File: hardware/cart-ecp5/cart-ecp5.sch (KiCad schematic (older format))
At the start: 1 part, among them U1 LFE5U-25F-xBG256x

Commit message: Create a basic N64 cartridge PCB layout
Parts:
- added C1: 10u, Capacitor_SMD:C_0603_1608Metric, symbol Device:C
- added C2: 10n, Capacitor_SMD:C_0402_1005Metric, symbol Device:C
- added C3, C4: 10u, Capacitor_SMD:C_0402_1005Metric, symbol Device:C
- added J1: N64_Cartridge_Bus, ng_n64:N64_Cartridge_Edge, symbol ng_n64:N64_Cartridge_Bus
- added L1: 470n, Inductor_SMD:L_0805_2012Metric, symbol Device:L
- added R1: 240R, Resistor_SMD:R_0603_1608Metric, symbol Device:R
- added R2, R3, R4: 100k, Resistor_SMD:R_0402_1005Metric, symbol Device:R
- added R5: 267k, Resistor_SMD:R_0402_1005Metric, symbol Device:R
- added U2: MT41K64M16TW-xxx, Package_BGA:BGA-96_9.0x13.0mm_Layout2x3x16_P0.8mm, symbol ng_memory:MT41K64M16TW-xxx
- added U3: FAN53541, Package_CSP:WLCSP-20_1.934x2.434mm_Layout4x5_P0.4mm, symbol ng_pmic:FAN53541
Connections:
- net labels added: DRAM_A0, DRAM_A1, DRAM_A10, DRAM_A11, DRAM_A12, DRAM_A13, DRAM_A14, DRAM_A15, DRAM_A2, DRAM_A3, DRAM_A4, DRAM_A5, DRAM_A6, DRAM_A7, DRAM_A8, DRAM_A9, DRAM_BA0, DRAM_BA1, DRAM_BA2, DRAM_CAS#, DRAM_CK+, DRAM_CK-, DRAM_CKE, DRAM_CS#, DRAM_DQ0, DRAM_DQ1, DRAM_DQ10, DRAM_DQ11, DRAM_DQ12, DRAM_DQ13, DRAM_DQ14, DRAM_DQ15, DRAM_DQ2, DRAM_DQ3, DRAM_DQ4, DRAM_DQ5, DRAM_DQ6, DRAM_DQ7, DRAM_DQ8, DRAM_DQ9, DRAM_LDM, DRAM_LDQS+, DRAM_LDQS-, DRAM_ODT, DRAM_RAS#, DRAM_RESET#, DRAM_UDM, DRAM_UDQS+, DRAM_UDQS-, DRAM_VDD, DRAM_VDDQ, DRAM_VREF, DRAM_WE#, DRAM_ZQ, FB1V1, N64_12V, N64_3V3, N64_AD0, N64_AD1, N64_AD10, N64_AD11, N64_AD12, N64_AD13, N64_AD14, N64_AD15, N64_AD2, N64_AD3, N64_AD4, N64_AD5, N64_AD6, N64_AD7, N64_AD8, N64_AD9, N64_ALE_H, N64_ALE_L, N64_AUDIO_L, N64_AUDIO_R, N64_COLD_RESET#, N64_OS_EVENT#, N64_READ#, N64_S_CLK, N64_S_DAT, N64_WRITE#, P3V3, PGOOD_1V1, SW1V1
- wire segments 235 -> 380
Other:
- moved on the sheet: U1A, U1B, U1C, U1D, U1E, U1F, U1G, U1H, U1I

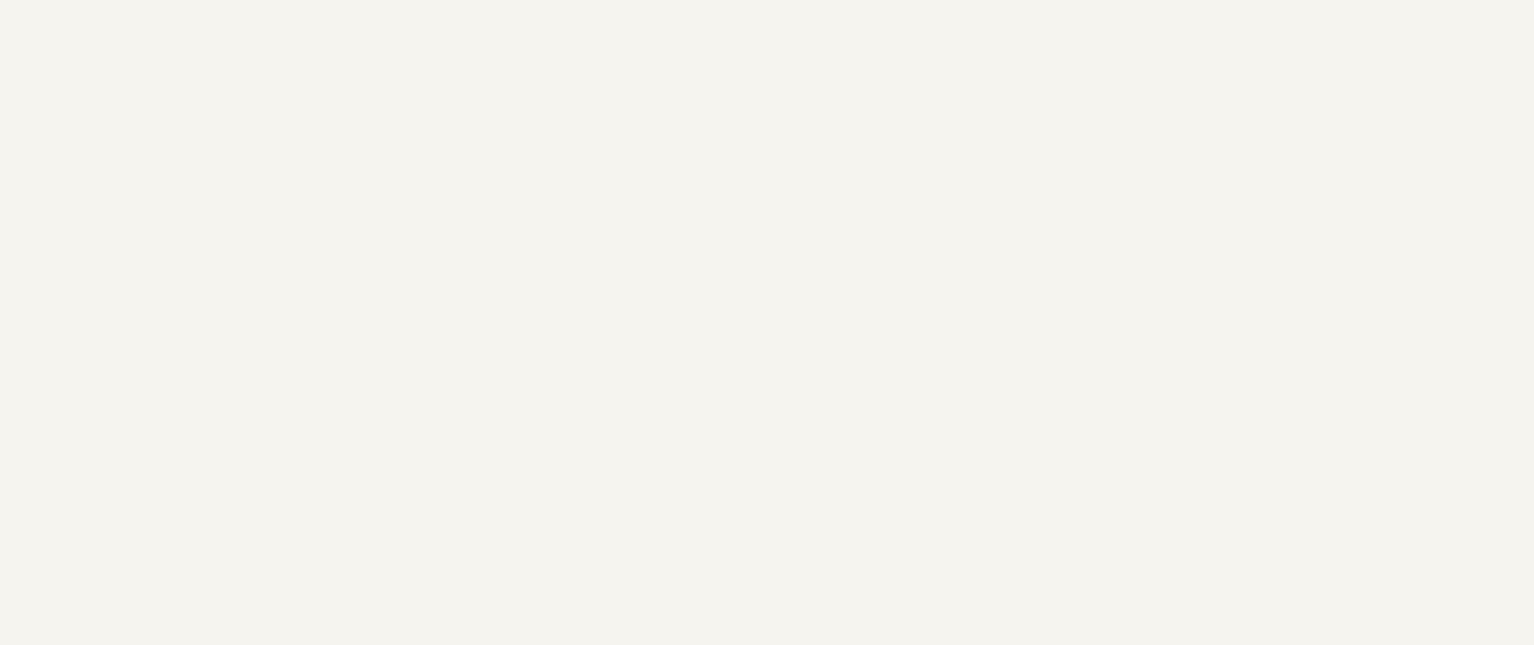
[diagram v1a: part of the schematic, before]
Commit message: Check new HyperRAM symbols on the board
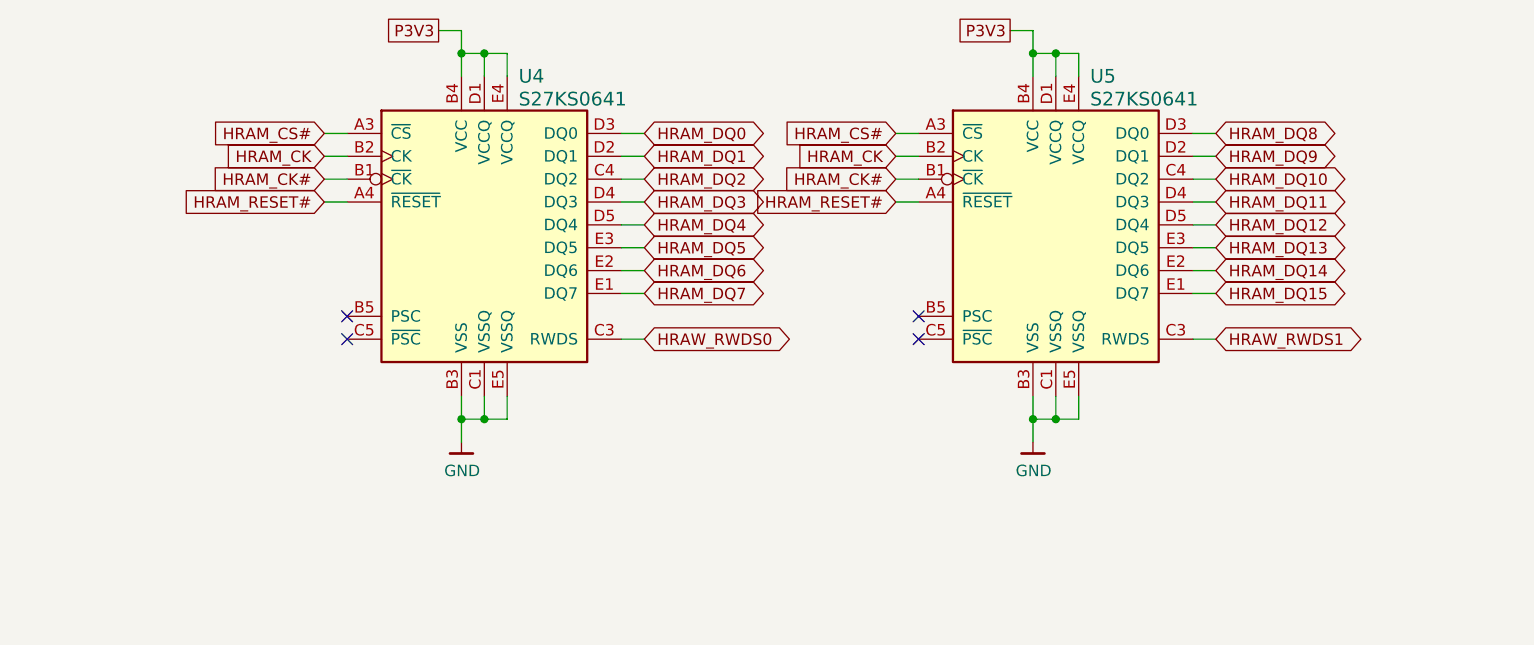
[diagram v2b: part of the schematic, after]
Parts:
- added U4, U5: S27KS0641, ng_package_bga:BGA-24_6.0x8.0mm_Layout5x5_P1.0mm_Pad0.4mm, symbol ng_memory:S27KS0641
- U1: footprint ng_package_bga:BGA-256_16x16_14.0x14.0mm_P0.8mm_Pad0.35mm -> ng_package_bga:BGA-256_14.0x14.0mm_Layout16x16_P0.8mm_Pad0.35mm
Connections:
- net labels added: HRAM_CK, HRAM_CK#, HRAM_CS#, HRAM_DQ0, HRAM_DQ1, HRAM_DQ10, HRAM_DQ11, HRAM_DQ12, HRAM_DQ13, HRAM_DQ14, HRAM_DQ15, HRAM_DQ2, HRAM_DQ3, HRAM_DQ4, HRAM_DQ5, HRAM_DQ6, HRAM_DQ7, HRAM_DQ8, HRAM_DQ9, HRAM_RESET#, HRAW_RWDS0, HRAW_RWDS1
- wire segments 380 -> 432
- no-connect marks 0 -> 4
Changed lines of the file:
@@
 F 0 "U1" H 3681 3553 60  0000 L CNN
 F 1 "LFE5U-25F-xBG256x" H 3681 3447 60  0000 L CNN
-F 2 "ng_package_bga:BGA-256_16x16_14.0x14.0mm_P0.8mm_Pad0.35mm" H 3300 3400 60  0001 R CNN
+F 2 "ng_package_bga:BGA-256_14.0x14.0mm_Layout16x16_P0.8mm_Pad0.35mm" H 3300 3400 60  0001 R CNN
 F 3 "" H 3300 3200 60  0001 R CNN
 F 4 "LFE5U-25F-xBG256x" H 3300 3300 60  0001 R CNN "MPN"
@@
 F 0 "U1" H 4031 5360 60  0000 L CNN
 F 1 "LFE5U-25F-xBG256x" H 4031 5254 60  0000 L CNN
-F 2 "ng_package_bga:BGA-256_16x16_14.0x14.0mm_P0.8mm_Pad0.35mm" H 2750 6100 60  0001 R CNN
+F 2 "ng_package_bga:BGA-256_14.0x14.0mm_Layout16x16_P0.8mm_Pad0.35mm" H 2750 6100 60  0001 R CNN
 F 3 "" H 2750 5900 60  0001 R CNN
 F 4 "LFE5U-25F-xBG256x" H 2750 6000 60  0001 R CNN "MPN"
@@
 F 0 "U1" H 7781 4860 60  0000 L CNN
 F 1 "LFE5U-25F-xBG256x" H 7781 4754 60  0000 L CNN
-F 2 "ng_package_bga:BGA-256_16x16_14.0x14.0mm_P0.8mm_Pad0.35mm" H 6500 6000 60  0001 R CNN
+F 2 "ng_package_bga:BGA-256_14.0x14.0mm_Layout16x16_P0.8mm_Pad0.35mm" H 6500 6000 60  0001 R CNN
 F 3 "" H 6500 5800 60  0001 R CNN
 F 4 "LFE5U-25F-xBG256x" H 6500 5900 60  0001 R CNN "MPN"
@@
 F 0 "U1" H 11731 4860 60  0000 L CNN
 F 1 "LFE5U-25F-xBG256x" H 11731 4754 60  0000 L CNN
-F 2 "ng_package_bga:BGA-256_16x16_14.0x14.0mm_P0.8mm_Pad0.35mm" H 9950 6000 60  0001 R CNN
+F 2 "ng_package_bga:BGA-256_14.0x14.0mm_Layout16x16_P0.8mm_Pad0.35mm" H 9950 6000 60  0001 R CNN
 F 3 "" H 9950 5800 60  0001 R CNN
 F 4 "LFE5U-25F-xBG256x" H 9950 5900 60  0001 R CNN "MPN"
@@
 F 0 "U1" H 15381 4610 60  0000 L CNN
 F 1 "LFE5U-25F-xBG256x" H 15381 4504 60  0000 L CNN
-F 2 "ng_package_bga:BGA-256_16x16_14.0x14.0mm_P0.8mm_Pad0.35mm" H 13600 5750 60  0001 R CNN
+F 2 "ng_package_bga:BGA-256_14.0x14.0mm_Layout16x16_P0.8mm_Pad0.35mm" H 13600 5750 60  0001 R CNN
 F 3 "" H 13600 5550 60  0001 R CNN
 F 4 "LFE5U-25F-xBG256x" H 13600 5650 60  0001 R CNN "MPN"
@@
 F 0 "U1" H 8431 9760 60  0000 L CNN
 F 1 "LFE5U-25F-xBG256x" H 8431 9654 60  0000 L CNN
-F 2 "ng_package_bga:BGA-256_16x16_14.0x14.0mm_P0.8mm_Pad0.35mm" H 6650 10900 60  0001 R CNN
+F 2 "ng_package_bga:BGA-256_14.0x14.0mm_Layout16x16_P0.8mm_Pad0.35mm" H 6650 10900 60  0001 R CNN
 F 3 "" H 6650 10700 60  0001 R CNN
 F 4 "LFE5U-25F-xBG256x" H 6650 10800 60  0001 R CNN "MPN"
@@
 F 0 "U1" H 12931 10260 60  0000 L CNN
 F 1 "LFE5U-25F-xBG256x" H 12931 10154 60  0000 L CNN
-F 2 "ng_package_bga:BGA-256_16x16_14.0x14.0mm_P0.8mm_Pad0.35mm" H 10950 10900 60  0001 R CNN
+F 2 "ng_package_bga:BGA-256_14.0x14.0mm_Layout16x16_P0.8mm_Pad0.35mm" H 10950 10900 60  0001 R CNN
 F 3 "" H 10950 10700 60  0001 R CNN
 F 4 "LFE5U-25F-xBG256x" H 10950 10800 60  0001 R CNN "MPN"
@@
 F 0 "U1" H 6831 3053 60  0000 L CNN
 F 1 "LFE5U-25F-xBG256x" H 6831 2947 60  0000 L CNN
-F 2 "ng_package_bga:BGA-256_16x16_14.0x14.0mm_P0.8mm_Pad0.35mm" H 6450 3200 60  0001 R CNN
+F 2 "ng_package_bga:BGA-256_14.0x14.0mm_Layout16x16_P0.8mm_Pad0.35mm" H 6450 3200 60  0001 R CNN
 F 3 "" H 6450 3000 60  0001 R CNN
 F 4 "LFE5U-25F-xBG256x" H 6450 3100 60  0001 R CNN "MPN"
@@
 F 0 "U1" H 4081 9560 60  0000 L CNN
 F 1 "LFE5U-25F-xBG256x" H 4081 9454 60  0000 L CNN
-F 2 "ng_package_bga:BGA-256_16x16_14.0x14.0mm_P0.8mm_Pad0.35mm" H 2300 10700 60  0001 R CNN
+F 2 "ng_package_bga:BGA-256_14.0x14.0mm_Layout16x16_P0.8mm_Pad0.35mm" H 2300 10700 60  0001 R CNN
 F 3 "" H 2300 10500 60  0001 R CNN
 F 4 "LFE5U-25F-xBG256x" H 2300 10600 60  0001 R CNN "MPN"
@@
 Wire Wire Line
 	2150 13550 2150 13650
+$Comp
+L ng_memory:S27KS0641 U5
+U 1 1 5F363B1F
+P 13600 2550
+F 0 "U5" H 13750 3300 60  0000 L CNN
+F 1 "S27KS0641" H 13750 3200 60  0000 L CNN
+F 2 "ng_package_bga:BGA-24_6.0x8.0mm_Layout5x5_P1.0mm_Pad0.4mm" H 12800 4500 60  0001 C CNN
+F 3 "https://www.cypress.com/file/183506/download" H 12800 4500 60  0001 C CNN
+	1    13600 2550
+	1    0    0    -1
+$EndComp
+Wire Wire Line
+	13500 3200 13500 3300
+Wire Wire Line
+	13500 3300 13600 3300
+Wire Wire Line
+	13700 3300 13700 3200
+Wire Wire Line
+	13600 3200 13600 3300
+Connection ~ 13600 3300
+Wire Wire Line
+	13600 3300 13700 3300
+Wire Wire Line
+	13500 3300 13500 3400
+Connection ~ 13500 3300
+Wire Wire Line
+	11000 3200 11000 3300
+Wire Wire Line
+	11000 3300 11100 3300
+Wire Wire Line
+	11200 3300 11200 3200
+Wire Wire Line
+	11100 3200 11100 3300
+Connection ~ 11100 3300
+Wire Wire Line
+	11100 3300 11200 3300
+$Comp
+L ng_memory:S27KS0641 U4
+U 1 1 5F363329
+P 11100 2550
+F 0 "U4" H 11250 3300 60  0000 L CNN
+F 1 "S27KS0641" H 11250 3200 60  0000 L CNN
+F 2 "ng_package_bga:BGA-24_6.0x8.0mm_Layout5x5_P1.0mm_Pad0.4mm" H 10300 4500 60  0001 C CNN
+F 3 "https://www.cypress.com/file/183506/download" H 10300 4500 60  0001 C CNN
+	1    11100 2550
+	1    0    0    -1
+$EndComp
+Wire Wire Line
+	11000 1800 11000 1700
+Wire Wire Line
+	11000 1700 11100 1700
+Wire Wire Line
+	11200 1700 11200 1800
+Wire Wire Line
+	11100 1800 11100 1700
+Connection ~ 11100 1700
+Wire Wire Line
+	11100 1700 11200 1700
+Wire Wire Line
+	13500 1800 13500 1700
+Wire Wire Line
+	13500 1700 13600 1700
+Wire Wire Line
+	13700 1700 13700 1800
+Wire Wire Line
+	13600 1800 13600 1700
+Connection ~ 13600 1700
+Wire Wire Line
+	13600 1700 13700 1700
+Wire Wire Line
+	11000 1700 11000 1600
+Connection ~ 11000 1700
+Wire Wire Line
+	11000 3300 11000 3400
+Connection ~ 11000 3300
+Wire Wire Line
+	13500 1700 13500 1600
+Connection ~ 13500 1700
+$Comp
+L ng_power:GND #PWR?
+U 1 1 5F5C81D3
+P 11000 3400
+F 0 "#PWR?" H 11000 3150 50  0001 C CNN
+F 1 "GND" H 11003 3274 50  0000 C CNN
+F 2 "" H 10900 3050 50  0001 C CNN
+F 3 "" H 11000 3400 50  0001 C CNN
+	1    11000 3400
+	1    0    0    -1
+$EndComp
+$Comp
+L ng_power:GND #PWR?
+U 1 1 5F5C9F5D
+P 13500 3400
+F 0 "#PWR?" H 13500 3150 50  0001 C CNN
+F 1 "GND" H 13503 3274 50  0000 C CNN
+F 2 "" H 13400 3050 50  0001 C CNN
+F 3 "" H 13500 3400 50  0001 C CNN
+	1    13500 3400
+	1    0    0    -1
+$EndComp
+Wire Wire Line
+	13500 1600 13400 1600
+Wire Wire Line
+	10900 1600 11000 1600
+Text GLabel 13400 1600 0    50   UnSpc ~ 0
+P3V3
+Text GLabel 10900 1600 0    50   UnSpc ~ 0
+P3V3
+Wire Wire Line
+	11700 2050 11800 2050
+Wire Wire Line
+	11700 2150 11800 2150
+Wire Wire Line
+	11700 2250 11800 2250
+Wire Wire Line
+	11700 2350 11800 2350
+Wire Wire Line
+	11700 2450 11800 2450
+Wire Wire Line
+	11700 2550 11800 2550
+Wire Wire Line
+	11700 2650 11800 2650
+Wire Wire Line
+	11700 2750 11800 2750
+Wire Wire Line
+	11700 2950 11800 2950
+Wire Wire Line
+	10500 2050 10400 2050
+Wire Wire Line
+	10500 2150 10400 2150
+Wire Wire Line
+	10500 2250 10400 2250
+Wire Wire Line
+	10500 2350 10400 2350
+Wire Wire Line
+	14200 2050 14300 2050
+Wire Wire Line
+	14200 2150 14300 2150
+Wire Wire Line
+	14200 2250 14300 2250
+Wire Wire Line
+	14200 2350 14300 2350
+Wire Wire Line
+	14200 2450 14300 2450
+Wire Wire Line
+	14200 2550 14300 2550
+Wire Wire Line
+	14200 2650 14300 2650
+Wire Wire Line
+	14200 2750 14300 2750
+Wire Wire Line
+	14200 2950 14300 2950
+Wire Wire Line
+	13000 2050 12900 2050
+Wire Wire Line
+	13000 2150 12900 2150
+Wire Wire Line
+	13000 2250 12900 2250
+Wire Wire Line
+	13000 2350 12900 2350
+Text GLabel 11800 2050 2    50   BiDi ~ 0
+HRAM_DQ0
+Text GLabel 11800 2150 2    50   BiDi ~ 0
+HRAM_DQ1
+Text GLabel 11800 2250 2    50   BiDi ~ 0
+HRAM_DQ2
+Text GLabel 11800 2350 2    50   BiDi ~ 0
+HRAM_DQ3
+Text GLabel 11800 2450 2    50   BiDi ~ 0
+HRAM_DQ4
+Text GLabel 11800 2550 2    50   BiDi ~ 0
+HRAM_DQ5
+Text GLabel 11800 2650 2    50   BiDi ~ 0
+HRAM_DQ6
+Text GLabel 11800 2750 2    50   BiDi ~ 0
+HRAM_DQ7
+Text GLabel 14300 2050 2    50   BiDi ~ 0
+HRAM_DQ8
+Text GLabel 14300 2150 2    50   BiDi ~ 0
+HRAM_DQ9
+Text GLabel 14300 2250 2    50   BiDi ~ 0
+HRAM_DQ10
+Text GLabel 14300 2350 2    50   BiDi ~ 0
+HRAM_DQ11
+Text GLabel 14300 2450 2    50   BiDi ~ 0
+HRAM_DQ12
+Text GLabel 14300 2550 2    50   BiDi ~ 0
+HRAM_DQ13
+Text GLabel 14300 2650 2    50   BiDi ~ 0
+HRAM_DQ14
+Text GLabel 14300 2750 2    50   BiDi ~ 0
+HRAM_DQ15
+Text GLabel 11800 2950 2    50   BiDi ~ 0
+HRAW_RWDS0
+Text GLabel 14300 2950 2    50   BiDi ~ 0
+HRAW_RWDS1
+NoConn ~ 13000 2850
+NoConn ~ 13000 2950
+NoConn ~ 10500 2850
+NoConn ~ 10500 2950
+Text GLabel 12900 2050 0    50   Input ~ 0
+HRAM_CS#
+Text GLabel 12900 2150 0    50   Input ~ 0
+HRAM_CK
+Text GLabel 12900 2250 0    50   Input ~ 0
+HRAM_CK#
+Text GLabel 12900 2350 0    50   Input ~ 0
+HRAM_RESET#
+Text GLabel 10400 2050 0    50   Input ~ 0
+HRAM_CS#
+Text GLabel 10400 2150 0    50   Input ~ 0
+HRAM_CK
+Text GLabel 10400 2250 0    50   Input ~ 0
+HRAM_CK#
+Text GLabel 10400 2350 0    50   Input ~ 0
+HRAM_RESET#
 $EndSCHEMATC

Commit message: Fill in basic ECP5 scaffolding
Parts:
- removed J1: N64_Cartridge_Bus, ng_n64:N64_Cartridge_Edge, symbol ng_n64:N64_Cartridge_Bus
- removed R1: 240R, Resistor_SMD:R_0603_1608Metric, symbol Device:R
- removed U1: LFE5U-25F-xBG256x, ng_package_bga:BGA-256_14.0x14.0mm_Layout16x16_P0.8mm_Pad0.35mm, symbol ng_fpga_lattice_ecp5:LFE5U-25F-xBG256x
- removed U2: MT41K64M16TW-xxx, Package_BGA:BGA-96_9.0x13.0mm_Layout2x3x16_P0.8mm, symbol ng_memory:MT41K64M16TW-xxx
- removed U4, U5: S27KS0641, ng_package_bga:BGA-24_6.0x8.0mm_Layout5x5_P1.0mm_Pad0.4mm, symbol ng_memory:S27KS0641
- added C? (x2): C, symbol Device:C
- added L?: L, symbol Device:L
- added R? (x2): R, symbol Device:R
- added U?: TLV62568DBV, Package_TO_SOT_SMD:SOT-23-5, symbol ng_regulator:TLV62568DBV
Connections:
- net labels removed: BANK0, BANK1, BANK2, BANK3, BANK6, BANK7, BANK8, DRAM_A0, DRAM_A1, DRAM_A10, DRAM_A11, DRAM_A12, DRAM_A13, DRAM_A14, DRAM_A15, DRAM_A2, DRAM_A3, DRAM_A4, DRAM_A5, DRAM_A6, DRAM_A7, DRAM_A8, DRAM_A9, DRAM_BA0, DRAM_BA1, DRAM_BA2, DRAM_CAS#, DRAM_CK+, DRAM_CK-, DRAM_CKE, DRAM_CS#, DRAM_DQ0, DRAM_DQ1, DRAM_DQ10, DRAM_DQ11, DRAM_DQ12, DRAM_DQ13, DRAM_DQ14, DRAM_DQ15, DRAM_DQ2, DRAM_DQ3, DRAM_DQ4, DRAM_DQ5, DRAM_DQ6, DRAM_DQ7, DRAM_DQ8, DRAM_DQ9, DRAM_LDM, DRAM_LDQS+, DRAM_LDQS-, DRAM_ODT, DRAM_RAS#, DRAM_RESET#, DRAM_UDM, DRAM_UDQS+, DRAM_UDQS-, DRAM_VDD, DRAM_VDDQ, DRAM_VREF, DRAM_WE#, DRAM_ZQ, HRAM_CK, HRAM_CK#, HRAM_CS#, HRAM_DQ0, HRAM_DQ1, HRAM_DQ10, HRAM_DQ11, HRAM_DQ12, HRAM_DQ13, HRAM_DQ14, HRAM_DQ15, HRAM_DQ2, HRAM_DQ3, HRAM_DQ4, HRAM_DQ5, HRAM_DQ6, HRAM_DQ7, HRAM_DQ8, HRAM_DQ9, HRAM_RESET#, HRAW_RWDS0, HRAW_RWDS1, JTAG, N64_12V, N64_3V3, N64_AD0, N64_AD1, N64_AD10, N64_AD11, N64_AD12, N64_AD13, N64_AD14, N64_AD15, N64_AD2, N64_AD3, N64_AD4, N64_AD5, N64_AD6, N64_AD7, N64_AD8, N64_AD9, N64_ALE_H, N64_ALE_L, N64_AUDIO_L, N64_AUDIO_R, N64_COLD_RESET#, N64_OS_EVENT#, N64_READ#, N64_S_CLK, N64_S_DAT, N64_WRITE#, P2V5, VCCIO0, VCCIO1, VCCIO2, VCCIO3, VCCIO6, VCCIO7, VCCIO8
- wire segments 432 -> 88
- no-connect marks 4 -> 0
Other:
- moved on the sheet: C1, C2, C3, C4, L1, R2, R3, R4, R5, U3
